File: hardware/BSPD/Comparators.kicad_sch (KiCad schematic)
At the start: 22 parts, among them U4 LM393B, U6 74HC2G14-Q100, U7 LM393B, U9 74HC1G32GV

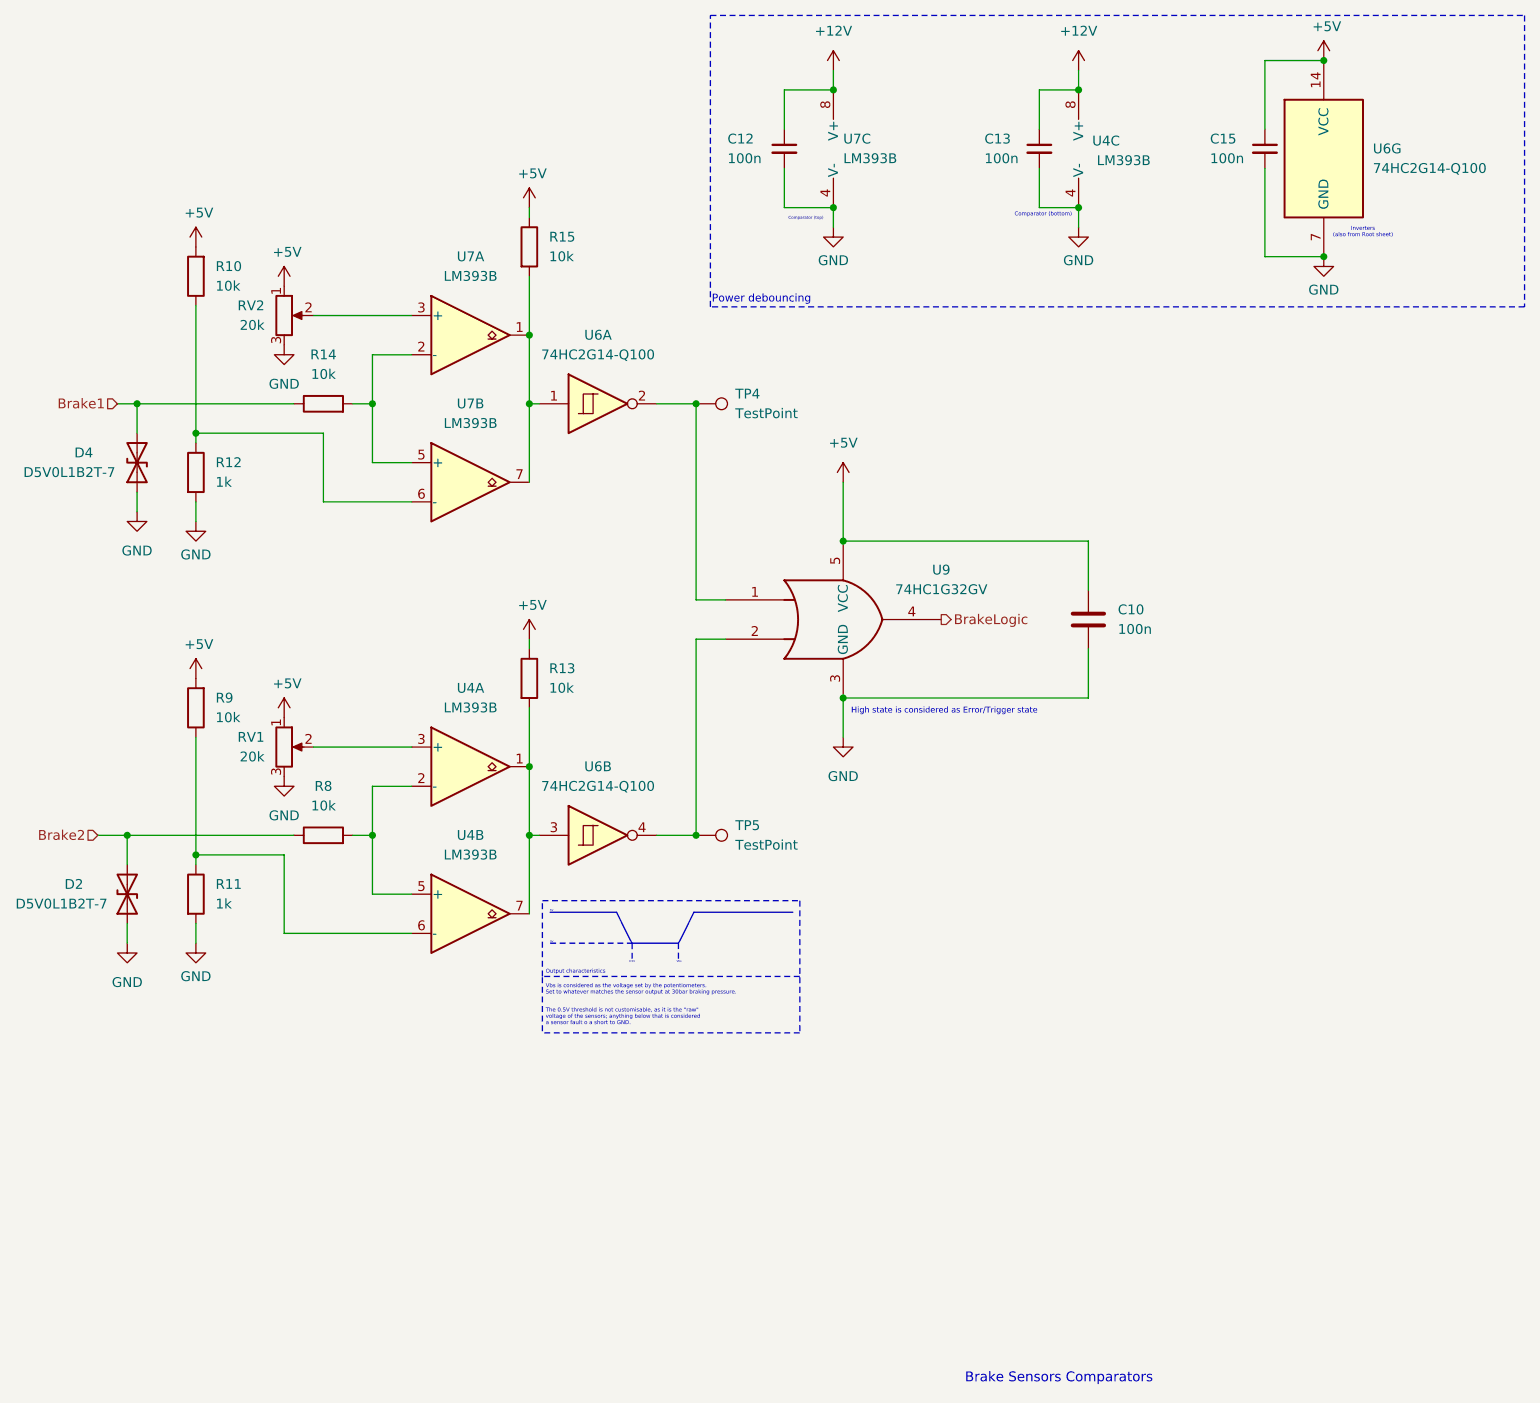
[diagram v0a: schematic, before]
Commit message: Fixed symbol errors
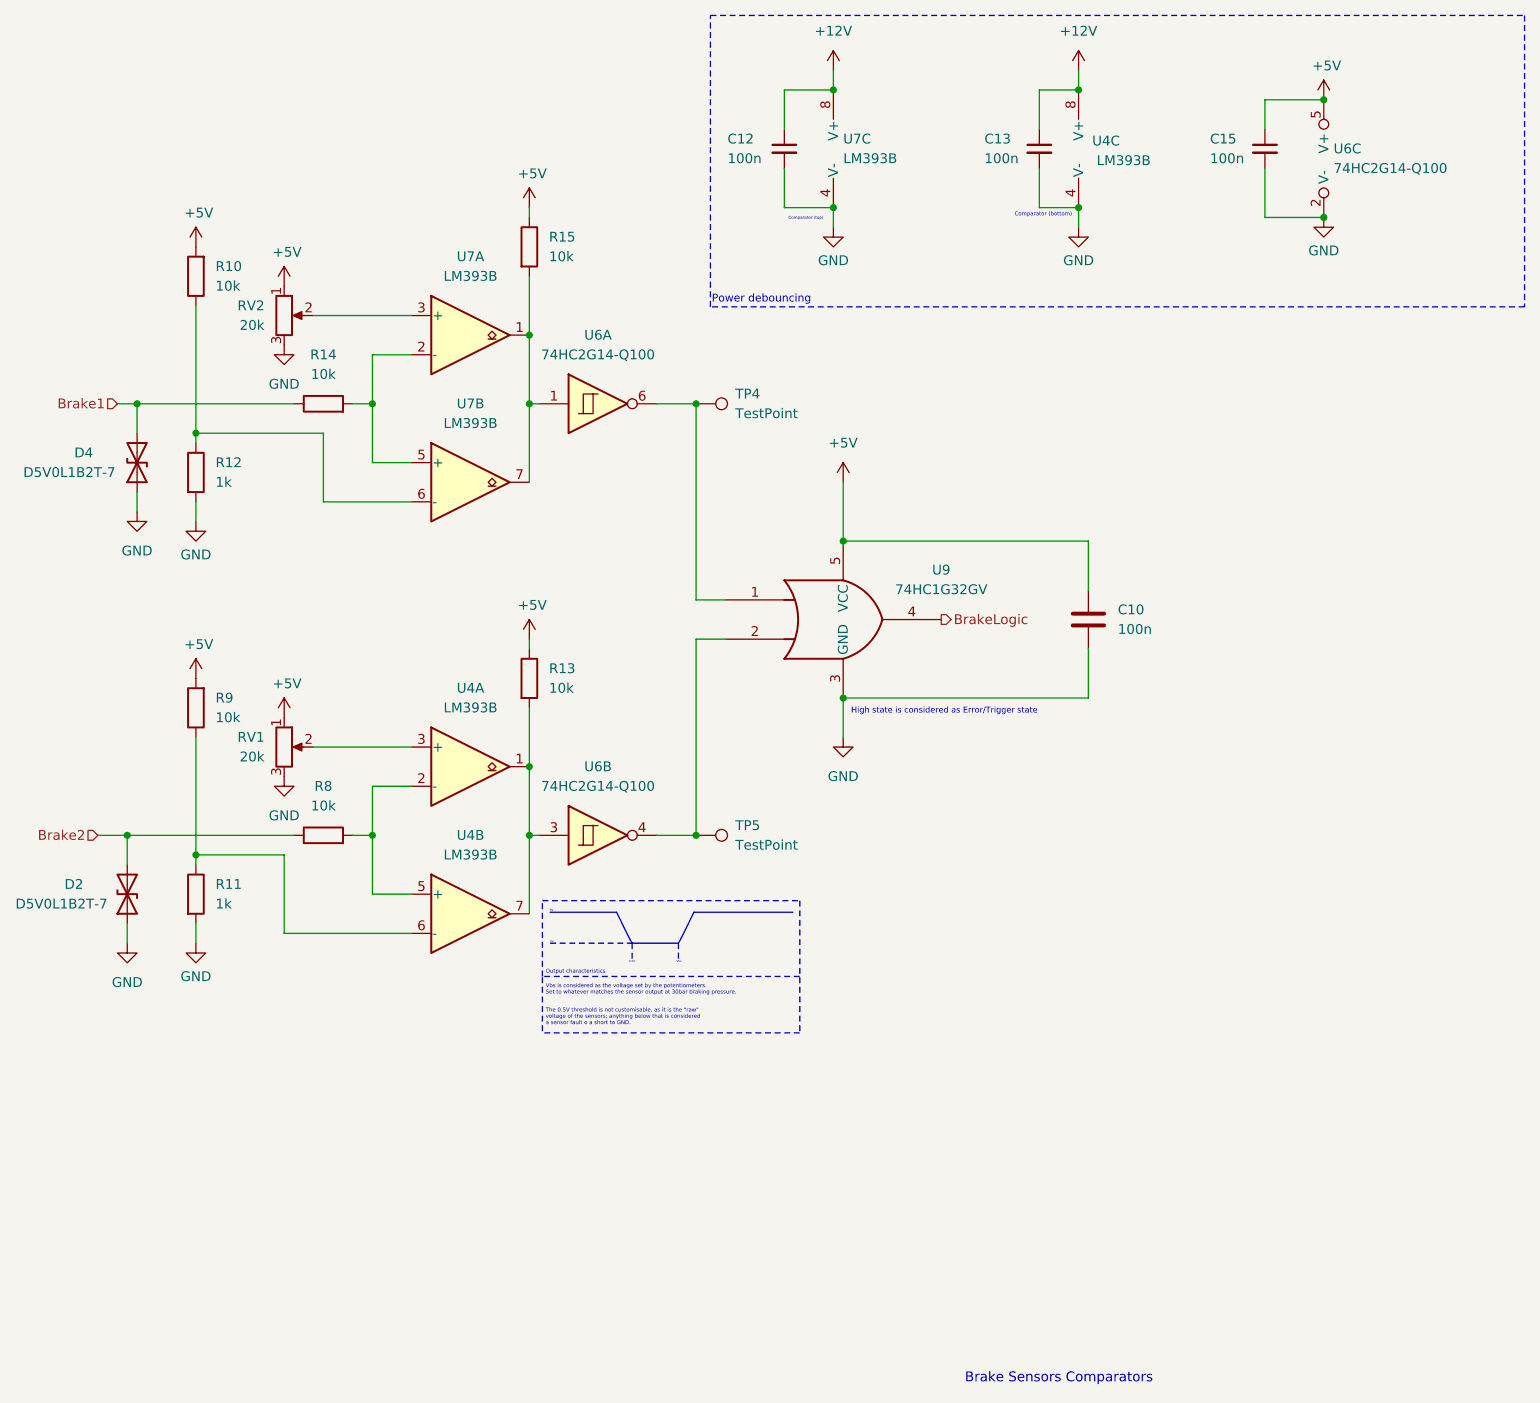
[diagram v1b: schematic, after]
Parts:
- removed U6: 74HC2G14-Q100, Package_TO_SOT_SMD:SOT-23-6, symbol 74xx:74HC14
- added U6: 74HC2G14-Q100, Package_SO:TSOP-6_1.65x3.05mm_P0.95mm, symbol 74HC:Inv_Schmitt
- U4, U7: footprint Package_SO:VSSOP-8_3x3mm_P0.65mm -> Package_SO:TSSOP-8_3x3mm_P0.65mm
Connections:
- net +5V: now also U6.5 (V+)
- net GND: now also U6.2 (V-)
- net at R15.2, U7.1, U7.7: now also U6.1
- net at TP4.1, U9.1: now also U6.6
- net at TP5.1, U9.2: now also U6.4
- net at R13.2, U4.1, U4.7: now also U6.3
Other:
- note removed: "Inverters (also from Root sheet)"

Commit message: Major changes. Read ext. description.
- Changed board to 4 layers due to trace fitment issues (or skill issues)
- Added mounting holes to be compatible with previous gen. of board
- Added unassigned footprints
- Fully fixed DRC errors
- Fixed comp. issues with schematic
- Added missing custom footprints to library (and made the library)
NOTE: Ignore "not matching with library copy" - It's matching. Trust me.
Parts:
- C10: footprint (none) -> Capacitor_SMD:C_0603_1608Metric_Pad1.08x0.95mm_HandSolder
- D2, D4: footprint (none) -> Diode_SMD:D_SOD-523
- TP4, TP5: footprint (none) -> TestPoint:TestPoint_Pad_D1.0mm
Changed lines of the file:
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@@
 			)
 		)
-		(property "Footprint" ""
+		(property "Footprint" "Diode_SMD:D_SOD-523"
 			(at 80.01 71.12 0)
 			(effects
@@
 			)
 		)
-		(property "Footprint" ""
+		(property "Footprint" "TestPoint:TestPoint_Pad_D1.0mm"
 			(at 152.4 124.46 0)
 			(effects
@@
 			)
 		)
-		(property "Footprint" ""
+		(property "Footprint" "Diode_SMD:D_SOD-523"
 			(at 78.74 127 0)
 			(effects
@@
 			)
 		)
-		(property "Footprint" ""
+		(property "Footprint" "TestPoint:TestPoint_Pad_D1.0mm"
 			(at 152.4 68.58 0)
 			(effects
@@
 			)
 		)
-		(property "Footprint" ""
+		(property "Footprint" "Capacitor_SMD:C_0603_1608Metric_Pad1.08x0.95mm_HandSolder"
 			(at 204.1652 95.25 0)
 			(effects

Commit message: CS gain fix, Added comments
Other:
- company: (none) -> Author:
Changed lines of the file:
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@@
 	(generator_version "9.0")
 	(paper "A4")
+	(title_block
+		(company "Author:")
+		(comment 1 "Reviewer: Przemysław Zioła, Piotr Lesicki")
+	)
 	(rectangle
 		(start 132.4964 127.8445)

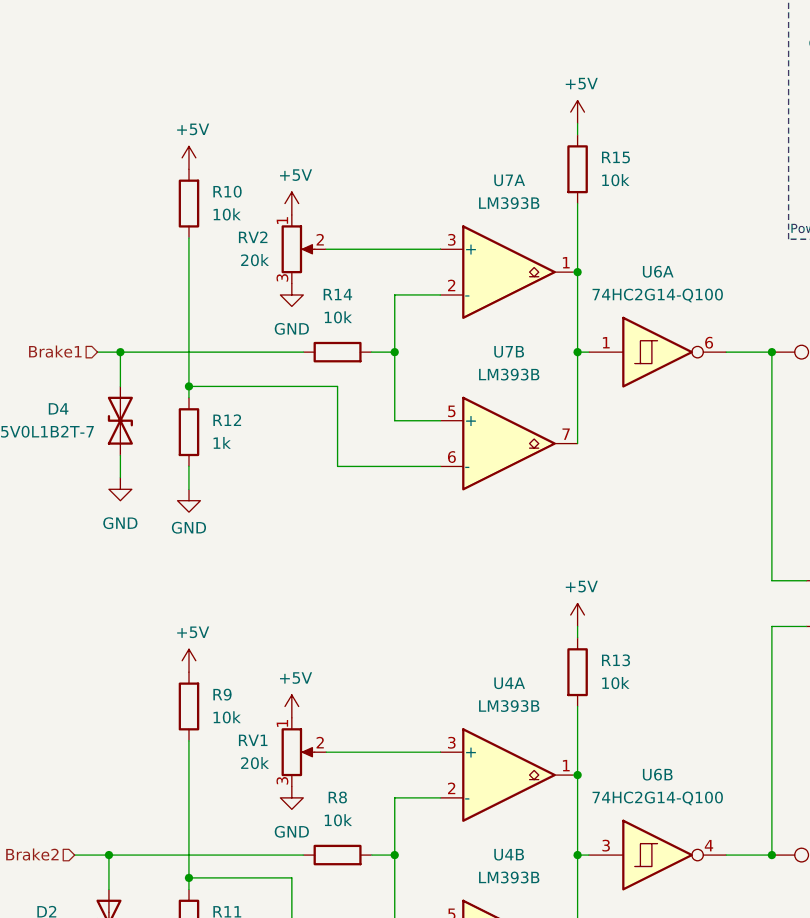
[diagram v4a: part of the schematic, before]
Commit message: Changes for 2026 Rules - added pull down resistors and reversed polarity of comparator (nie pozdrawiam Zdrajcy)
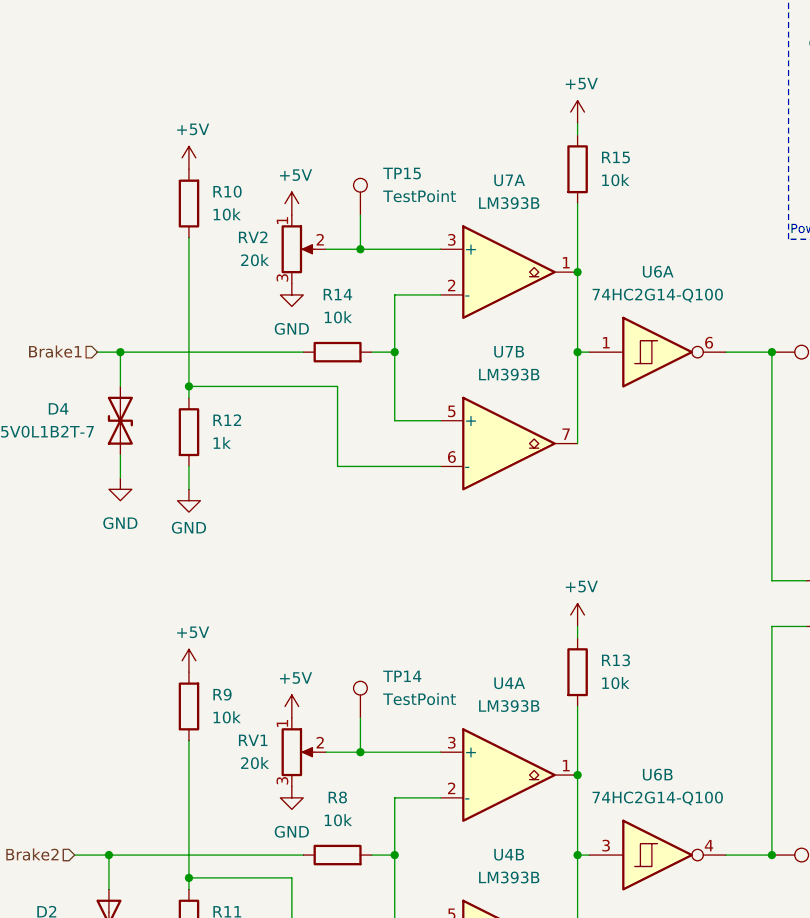
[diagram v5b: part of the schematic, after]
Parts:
- added TP14, TP15: TestPoint, TestPoint:TestPoint_Pad_D1.0mm, symbol Connector:TestPoint
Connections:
- net at RV2.2, U7.3 (+): now also TP15.1
- net at RV1.2, U4.3 (+): now also TP14.1
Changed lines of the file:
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@@
 	)
 	(junction
+		(at 106.68 52.07)
+		(diameter 0)
+		(color 0 0 0 0)
+	)
+	(junction
 		(at 110.49 119.38)
 		(diameter 0)
@@
 	)
 	(junction
+		(at 106.68 107.95)
+		(diameter 0)
+		(color 0 0 0 0)
+	)
+	(junction
 		(at 170.18 38.1)
 		(diameter 0)
@@
 	(wire
 		(pts
+			(xy 106.68 52.07) (xy 115.57 52.07)
+		)
+		(stroke
+			(width 0)
+			(type default)
+		)
+	)
+	(wire
+		(pts
 			(xy 170.18 22.86) (xy 163.83 22.86)
 		)
@@
 	(wire
 		(pts
-			(xy 102.87 52.07) (xy 115.57 52.07)
+			(xy 102.87 52.07) (xy 106.68 52.07)
 		)
 		(stroke
@@
 	(wire
 		(pts
+			(xy 106.68 48.26) (xy 106.68 52.07)
+		)
+		(stroke
+			(width 0)
+			(type default)
+		)
+	)
+	(wire
+		(pts
 			(xy 77.47 63.5) (xy 80.01 63.5)
 		)
@@
 	(wire
 		(pts
-			(xy 102.87 107.95) (xy 115.57 107.95)
+			(xy 102.87 107.95) (xy 106.68 107.95)
 		)
 		(stroke
@@
 	(wire
 		(pts
+			(xy 106.68 104.14) (xy 106.68 107.95)
+		)
+		(stroke
+			(width 0)
+			(type default)
+		)
+	)
+	(wire
+		(pts
 			(xy 201.93 40.64) (xy 201.93 38.1)
 		)
@@
 	(wire
 		(pts
+			(xy 106.68 107.95) (xy 115.57 107.95)
+		)
+		(stroke
+			(width 0)
+			(type default)
+		)
+	)
+	(wire
+		(pts
 			(xy 87.63 133.35) (xy 87.63 130.81)
 		)
@@
 	)
 	(symbol
+		(lib_id "Connector:TestPoint")
+		(at 106.68 48.26 0)
+		(unit 1)
+		(exclude_from_sim no)
+		(in_bom yes)
+		(on_board yes)
+		(dnp no)
+		(fields_autoplaced yes)
+		(property "Reference" "TP15"
+			(at 109.22 43.6879 0)
+			(effects
+				(font
+					(size 1.27 1.27)
+				)
+				(justify left)
+			)
+		)
+		(property "Value" "TestPoint"
+			(at 109.22 46.2279 0)
+			(effects
+				(font
+					(size 1.27 1.27)
+				)
+				(justify left)
+			)
+		)
+		(property "Footprint" "TestPoint:TestPoint_Pad_D1.0mm"
+			(at 111.76 48.26 0)
+			(effects
+				(font
+					(size 1.27 1.27)
+				)
+				(hide yes)
+			)
+		)
+		(property "Datasheet" "~"
+			(at 111.76 48.26 0)
+			(effects
+				(font
+					(size 1.27 1.27)
+				)
+				(hide yes)
+			)
+		)
+		(property "Description" "test point"
+			(at 106.68 48.26 0)
+			(effects
+				(font
+					(size 1.27 1.27)
+				)
+				(hide yes)
+			)
+		)
+		(pin "1"
+		)
+		(instances
+			(project "PUTM_EV_BSPD_2025"
+				(path "/b652b05a-4e3d-4ad1-b032-18886abe7d45/743c9fc1-2f1a-4d5a-9140-72b33986ce8b"
+					(reference "TP15")
+					(unit 1)
+				)
+			)
+		)
+	)
+	(symbol
 		(lib_id "power:GND")
 		(at 99.06 55.88 0)
@@
 					(unit 1)
 				)
+			)
+		)
+	)
+	(symbol
+		(lib_id "Connector:TestPoint")
+		(at 106.68 104.14 0)
+		(unit 1)
+		(exclude_from_sim no)
+		(in_bom yes)
+		(on_board yes)
+		(dnp no)
+		(fields_autoplaced yes)
+		(property "Reference" "TP14"
+			(at 109.22 99.5679 0)
+			(effects
+				(font
+					(size 1.27 1.27)
+				)
+				(justify left)
+			)
+		)
+		(property "Value" "TestPoint"
+			(at 109.22 102.1079 0)
+			(effects
+				(font
+					(size 1.27 1.27)
+				)
+				(justify left)
+			)
+		)
+		(property "Footprint" "TestPoint:TestPoint_Pad_D1.0mm"
+			(at 111.76 104.14 0)
+			(effects
+				(font
+					(size 1.27 1.27)
+				)
+				(hide yes)
+			)
+		)
+		(property "Datasheet" "~"
+			(at 111.76 104.14 0)
+			(effects
+				(font
+					(size 1.27 1.27)
+				)
+				(hide yes)
+			)
+		)
+		(property "Description" "test point"
+			(at 106.68 104.14 0)
+			(effects
+				(font
+					(size 1.27 1.27)
+				)
+				(hide yes)
+			)
+		)
+		(pin "1"
+		)
+		(instances
+			(project "PUTM_EV_BSPD_2025"
+				(path "/b652b05a-4e3d-4ad1-b032-18886abe7d45/743c9fc1-2f1a-4d5a-9140-72b33986ce8b"
+					(reference "TP14")
+					(unit 1)
+				)
